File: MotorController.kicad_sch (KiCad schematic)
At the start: 120 parts, among them IC1 ft234xd, IC2 A3921KLPTR-T, IC3 A3921KLPTR-T, J1 SH, J10 XT30, J2 USB_B_Micro, J3 Conn_01x02, J4 Conn_01x04, J5 3020-10-0300-00, J6 SH, J7 SH, J8 Conn_01x02, J9 3020-10-0300-00, Q1 GSFQ6806, Q2 GSFQ6806, Q3 GSFQ6806, Q4 GSFQ6806, Q5 Q_PMOS_GDSD, SW1 SW_Push, SW2 SW_MEC_5E, SW3 Emergency, SW4 SW_MEC_5E, SW5 SW_SPDT, U1 LXES11D, U2 STM32F303K8Tx, U3 TJA1441AT, U4 TPSM13604HNDWR, U5 LMZ12002EXT, Y1 32M

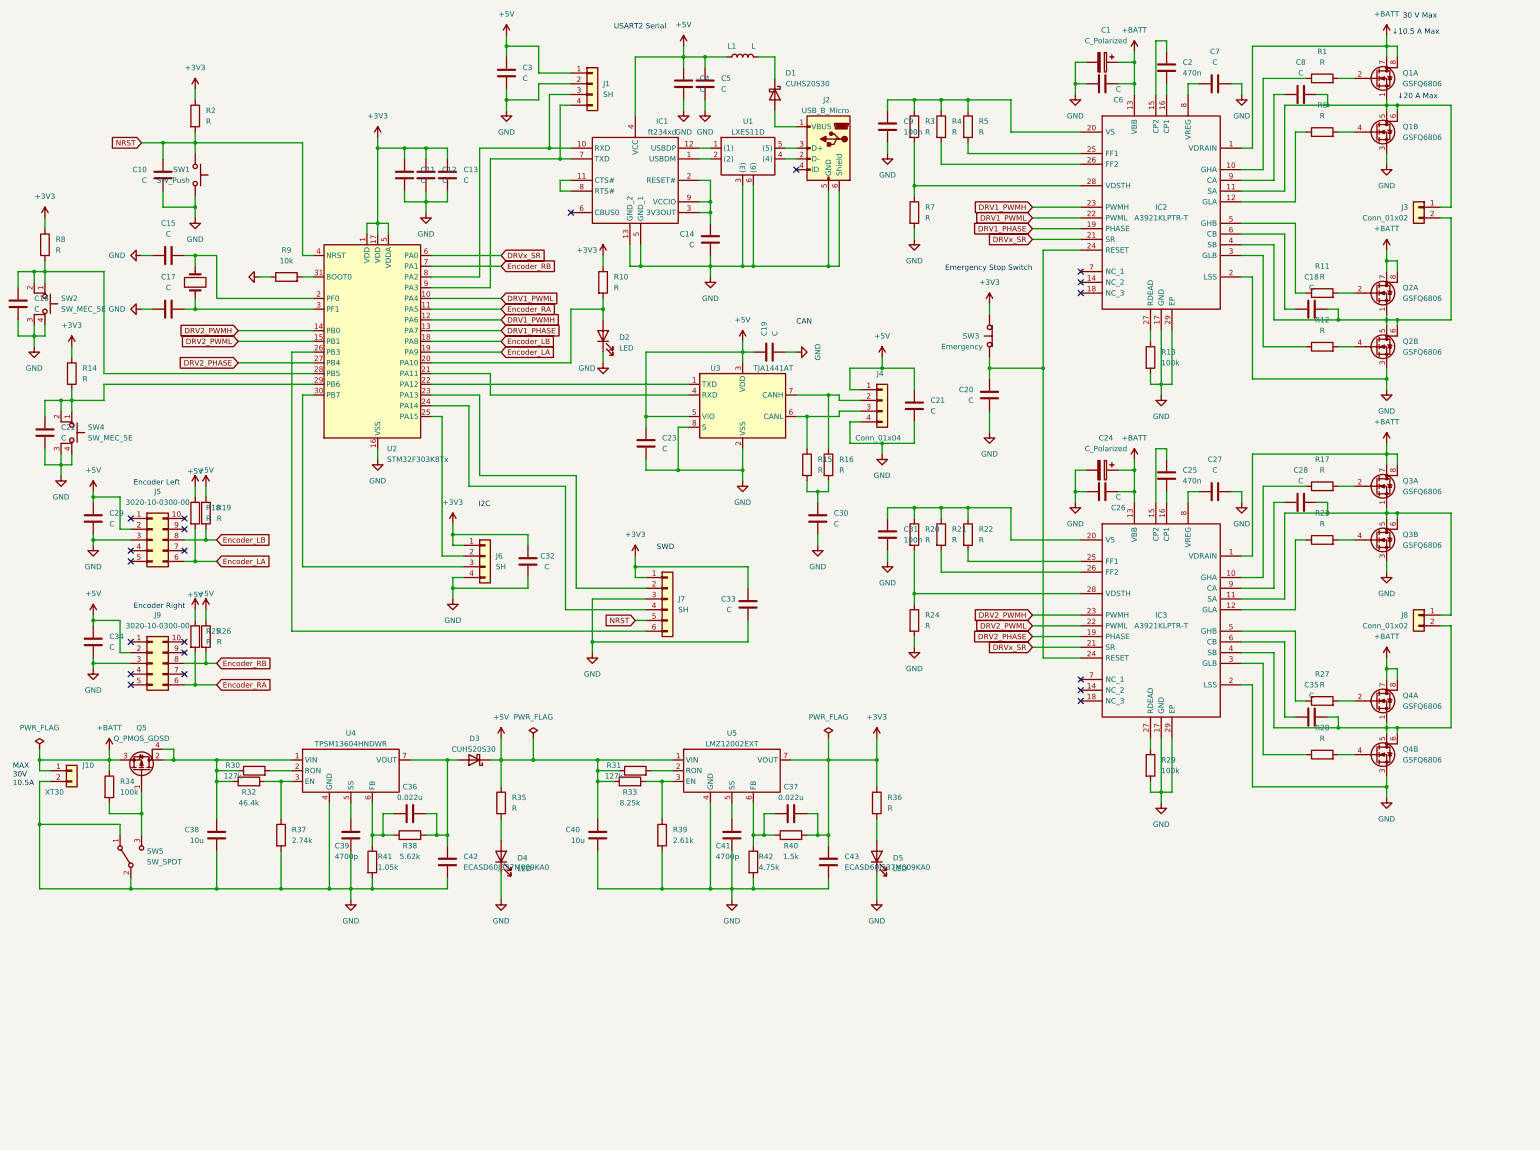
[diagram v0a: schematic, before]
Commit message: DCDC の出力コンデンサの記号を有極性にした。H ブリッジ FET にダイオード外付けした。A3921 のリセットピンと CPU のリセットピンを共有した。安全停止をモータの電力供給の手前に追加した。安全停止を Pch FET で実現しようとした。Pch FET の型番決めた
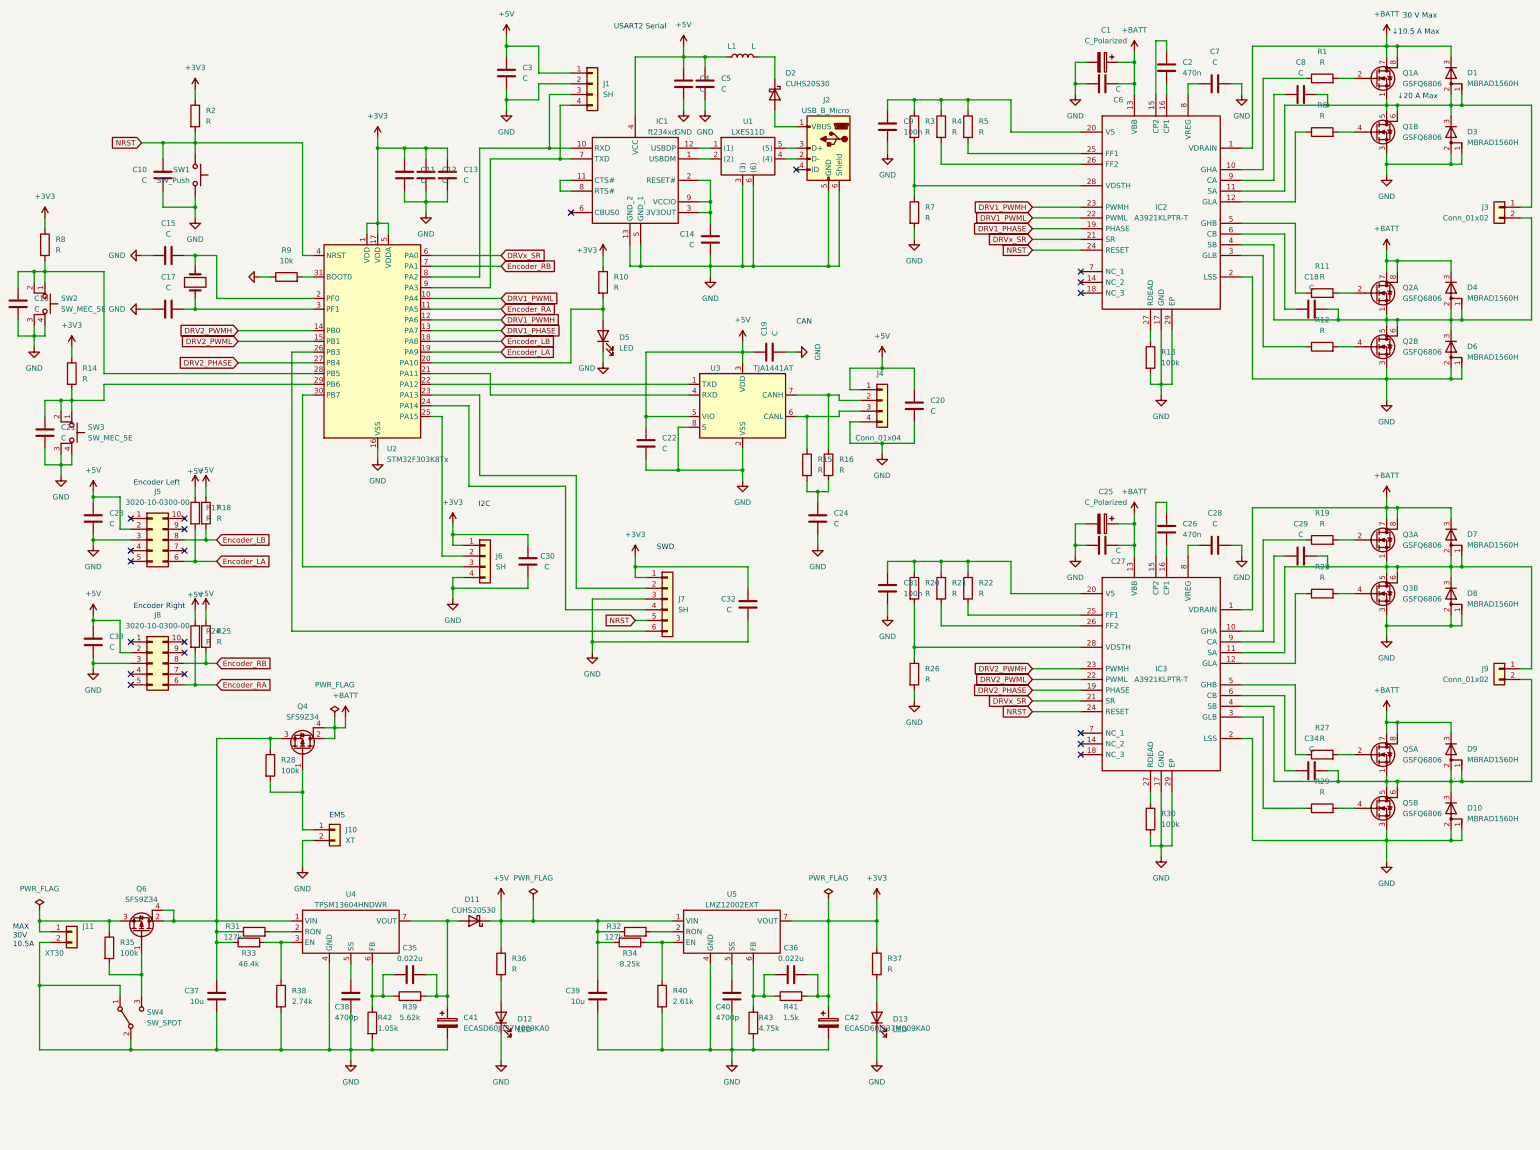
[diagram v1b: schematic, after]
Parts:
- removed C20: C, symbol Device:C
- removed SW3: Emergency, symbol Switch:SW_Push_Open
- added D1, D10, D3, D4, D6, D7, D8, D9: MBRAD1560H, symbol Device:D_AAK
- added J10: XT, symbol Connector_Generic:Conn_01x02
- added Q4: SFS9Z34, symbol Device:Q_PMOS_GDSD
- added R28: 100k, symbol Device:R
- C41: renamed from C42; symbol Device:C -> Device:C_Polarized
- C42: renamed from C43; symbol Device:C -> Device:C_Polarized
- Q6: renamed from Q5; value Q_PMOS_GDSD -> SFS9Z34
- renumbered C21 to C20, C22 to C21, C23 to C22, C29 to C23, C30 to C24, C24 to C25, C25 to C26, C26 to C27, C27 to C28, C28 to C29, C32 to C30, C33 to C32, C34 to C33, C35 to C34, C36 to C35, C37 to C36, C38 to C37, C39 to C38, C40 to C39, C41 to C40, D3 to D11, D4 to D12, D5 to D13, D1 to D2, D2 to D5, J10 to J11, J9 to J8, J8 to J9, Q4 to Q5, R18 to R17, R19 to R18, R17 to R19, R25 to R24, R26 to R25, R24 to R26, R28 to R29, R29 to R30, R30 to R31, R31 to R32, R32 to R33, R33 to R34, R34 to R35, R35 to R36, R36 to R37, R37 to R38, R38 to R39, R39 to R40, R40 to R41, R41 to R42, R42 to R43, SW4 to SW3, SW5 to SW4
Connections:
- net +BATT: now also D1.3 (K), D4.3 (K), D7.3 (K), D9.3 (K), Q4.2 (D), Q4.4 (D); no longer J11.1 (Pin_1), Q6.3 (S), R35.1
- net GND: now also D10.1 (A), D10.2 (A), D3.1 (A), D3.2 (A), D6.1 (A), D6.2 (A), D8.1 (A), D8.2 (A), J10.2 (Pin_2)
- net NRST: now also IC2.24 (RESET), IC3.24 (RESET)
- net at C29.1, IC3.11 (SA), J9.1 (Pin_1)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: now also D7.1 (A), D7.2 (A), D8.3 (K)
- net at C18.1, IC2.4 (SB), J3.2 (Pin_2)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: now also D4.1 (A), D4.2 (A), D6.3 (K)
- net at C34.1, IC3.4 (SB), J9.2 (Pin_2)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: now also D10.3 (K), D9.1 (A), D9.2 (A)
- net at C37.1, Q6.2 (D), Q6.4 (D)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: now also Q4.3 (S), R28.1
- net at C8.1, IC2.11 (SA), J3.1 (Pin_1)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: now also D1.1 (A), D1.2 (A), D3.3 (K)
- new net: J11.1 (Pin_1), Q6.3 (S), R35.1
- new net: J10.1 (Pin_1), Q4.1 (G), R28.2
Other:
- note added: "EMS"
- note removed: "Emergency Stop Switch"
- moved on the sheet: C25, C26, C27, C28, C29, C31, C34, C35, C36, C37, C38, C39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

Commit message: フットプリントの更新
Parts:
- removed SW1: SW_Push, symbol Switch:SW_Push
- added SW5: SW_MEC_5E, symbol Switch:SW_MEC_5E
- C10, C11, C12, C13, C14, C15, C16, C17, C18, C19, C2, C20, C21, C22, C23, C24, C26, C27, C28, C29, C3, C30, C31, C32, C33, C34, C35, C36, C37, C38, C39, C4, C40, C5, C6, C7, C8, C9: footprint (none) -> Capacitor_SMD:C_0603_1608Metric
- C41, C42: footprint (none) -> LibraryLoader:CAPPM7343X310N
- D11, D2: footprint Diode_SMD:D_MELF -> LibraryLoader:CUHS20S40H3F
- D12, D13, D5: footprint (none) -> LED_SMD:LED_0603_1608Metric
- J10, J11: footprint (none) -> LibraryLoader:XT30PWF
- J2: footprint (none) -> Connector_USB:USB_Micro-B_Amphenol_10118194_Horizontal
- L1: value L -> BLM18PG600SN1D; footprint (none) -> Inductor_SMD:L_0603_1608Metric
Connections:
- net GND: now also SW5.3 (K), SW5.4 (A)
- net NRST: now also SW5.1, SW5.2

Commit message: フットプリント再更新
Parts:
- Q1, Q2, Q3, Q5: footprint (none) -> Package_SO:HSOP-8-1EP_3.9x4.9mm_P1.27mm_EP2.3x2.3mm
- R1, R10, R11, R12, R13, R14, R15, R16, R17, R18, R19, R2, R20, R21, R22, R23, R24, R25, R26, R27, R28, R29, R3, R30, R31, R32, R33, R34, R35, R36, R37, R38, R39, R4, R40, R41, R42, R43, R5, R6, R7, R8, R9: footprint (none) -> Resistor_SMD:R_0603_1608Metric
- U1: footprint (none) -> LibraryLoader:LXES11DAA2135
- U4, U5: footprint (none) -> Package_TO_SOT_SMD:Texas_NDW-7_TabPin8

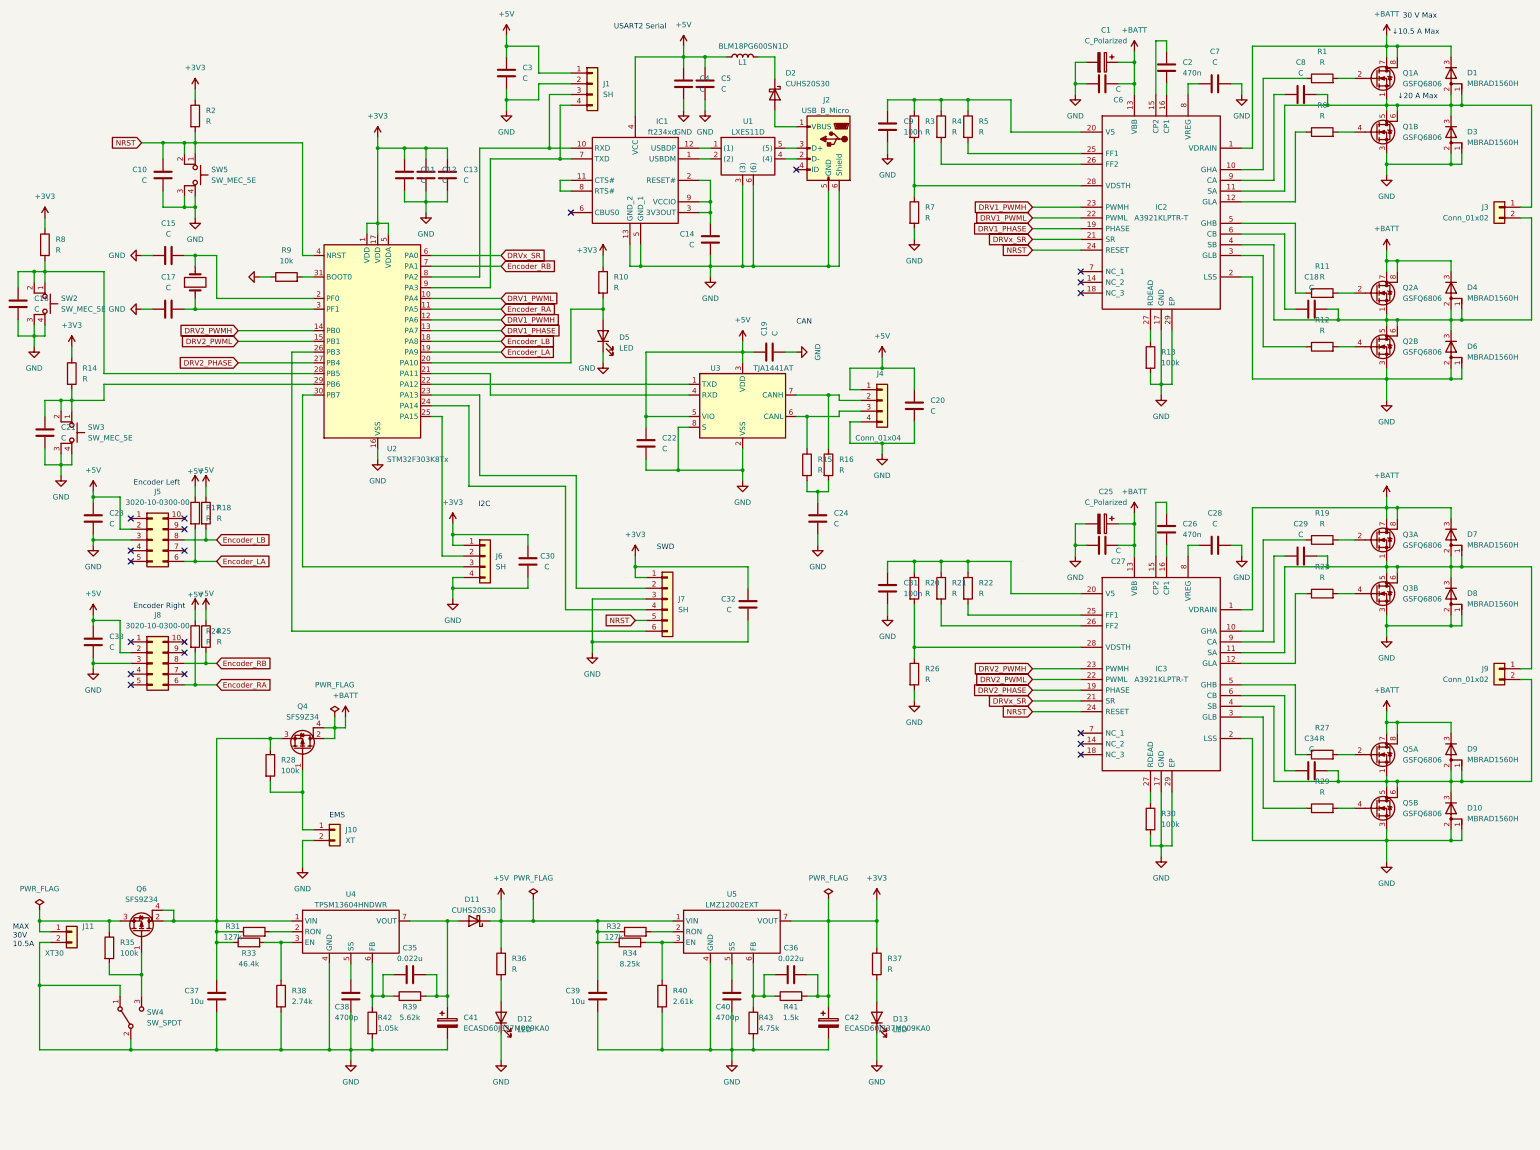
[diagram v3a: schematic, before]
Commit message: 追加パーツ含めてアノテーション全部終わらせた。フットプリントをグループごとに分類して分けて設置した
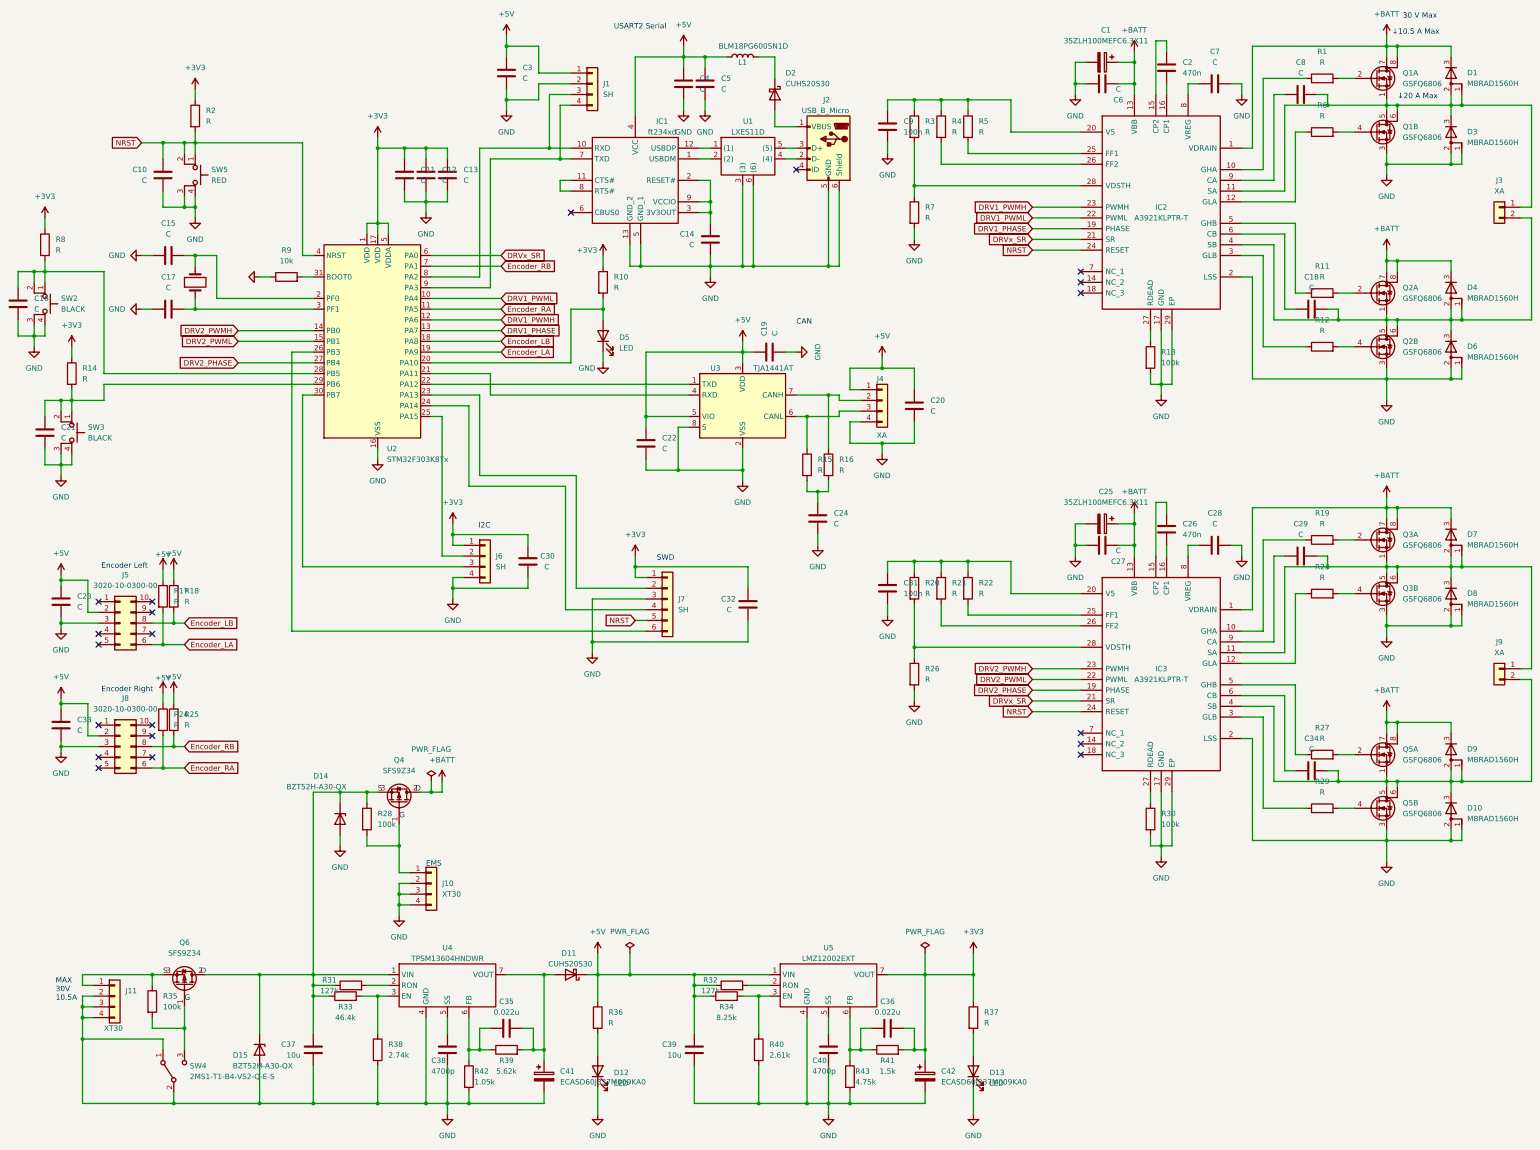
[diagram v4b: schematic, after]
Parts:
- added D14, D15: BZT52H-A30-QX, Diode_SMD:D_1206_3216Metric, symbol Device:D_Zener
- C1, C25: value C_Polarized -> 35ZLH100MEFC6.3X11; footprint (none) -> Capacitor_THT:CP_Radial_D6.3mm_P2.50mm
- D1, D10, D3, D4, D6, D7, D8, D9: footprint (none) -> LibraryLoader:DIO_MBRAD1560H
- J1, J6: footprint (none) -> Connector_JST:JST_SH_BM04B-SRSS-TB_1x04-1MP_P1.00mm_Vertical
- J10: value XT -> XT30; footprint LibraryLoader:XT30PWF -> LibraryLoader:XT30PWM; symbol Connector_Generic:Conn_01x02 -> Connector_Generic:Conn_01x04
- J11: footprint LibraryLoader:XT30PWF -> LibraryLoader:XT30PWM; symbol Connector_Generic:Conn_01x02 -> Connector_Generic:Conn_01x04
- J3, J9: value Conn_01x02 -> XA; footprint (none) -> Connector_JST:JST_XA_B02B-XASK-1-A_1x02_P2.50mm_Vertical
- J4: value Conn_01x04 -> XA; footprint (none) -> Connector_JST:JST_XA_B04B-XASK-1-A_1x04_P2.50mm_Vertical
- J5, J8: footprint (none) -> Connector_IDC:IDC-Header_2x10_P2.54mm_Vertical
- J7: footprint (none) -> Connector_JST:JST_SH_BM06B-SRSS-TB_1x06-1MP_P1.00mm_Vertical
- Q4, Q6: footprint (none) -> Package_TO_SOT_THT:TO-220F-3_Horizontal_TabDown; symbol Device:Q_PMOS_GDSD -> Device:Q_PMOS_GDS
- SW2, SW3: value SW_MEC_5E -> BLACK; footprint (none) -> LibraryLoader:DTS-63-N-V-BLK(TS-0606-F-N
- SW4: value SW_SPDT -> 2MS1-T1-B4-VS2-Q-E-S; footprint (none) -> LibraryLoader:2MS1-T1-B4-VS2-Q-E-S
- SW5: value SW_MEC_5E -> RED; footprint (none) -> LibraryLoader:DTS-63-N-V-BLK(TS-0606-F-N
- Y1: footprint (none) -> Crystal:Crystal_HC49-4H_Vertical
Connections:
- net +BATT: no longer Q4.4 (D)
- net GND: now also J10.3 (Pin_3), J10.4 (Pin_4), J11.3 (Pin_3), J11.4 (Pin_4), D14.2 (A), D15.2 (A)
- net at C37.1, Q4.3 (S), Q6.2 (D)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: now also D14.1 (K), D15.1 (K); no longer Q6.4 (D)
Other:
- note added: "D"
- note added: "G"
- note added: "S"
- moved on the sheet: C23, C33, C35, C36, C37, C38, C39, C40, C41, C42, D11, D12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
